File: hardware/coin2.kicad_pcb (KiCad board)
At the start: 2 copper layers, 140 x 40 mm, 69 parts, among them J1 Conn_01x04, J2 Conn_01x03, T1 TestPoint_THTPad_3.0x3.0mm_Dr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, T12 TestPoint_THTPad_3.0x3.0mm_Dr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, T13 TestPoint_THTPad_3.0x3.0mm_Dr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, T14 TestPoint_THTPad_3.0x3.0mm_Dr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, T15 TestPoint_THTPad_3.0x3.0mm_Dr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, T16 TestPoint_THTPad_3.0x3.0mm_Dr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, T18 TestPoint_THTPad_3.0x3.0mm_Dr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, T19 TestPoint_THTPad_3.0x3.0mm_Dr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, T20 TestPoint_THTPad_3.0x3.0mm_Dr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, T21 TestPoint_THTPad_3.0x3.0mm_Dr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, T22 TestPoint_THTPad_3.0x3.0mm_Dr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, T41 TestPoint_THTPad_D1.0mm_Drill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, T42 TestPoint_THTPad_D1.0mm_Drill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, T43 TestPoint_THTPad_D1.0mm_Drill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, T44 TestPoint_THTPad_D1.0mm_Drill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, T45 TestPoint_THTPad_D1.0mm_Drill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, T46 TestPoint_THTPad_D1.0mm_Drill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, T47 TestPoint_THTPad_D1.0mm_Drill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, T48 TestPoint_THTPad_D1.0mm_Drill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, T49 TestPoint_THTPad_D1.0mm_Drill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, T50 TestPoint_THTPad_D1.0mm_Drill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, T51 TestPoint_THTPad_D1.0mm_Drill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, T51 TestPoint_THTPad_D2.0mm_Drill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, T52 TestPoint_THTPad_D1.0mm_Drill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, T52 TestPoint_THTPad_D2.0mm_Drill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, T53 TestPoint_THTPad_D2.0mm_Drill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, T54 TestPoint_THTPad_D2.0mm_Drill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, T55 TestPoint_THTPad_D2.0mm_Drill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, T56 TestPoint_THTPad_D2.0mm_Drill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, U1 WCH CH32V003F4U6

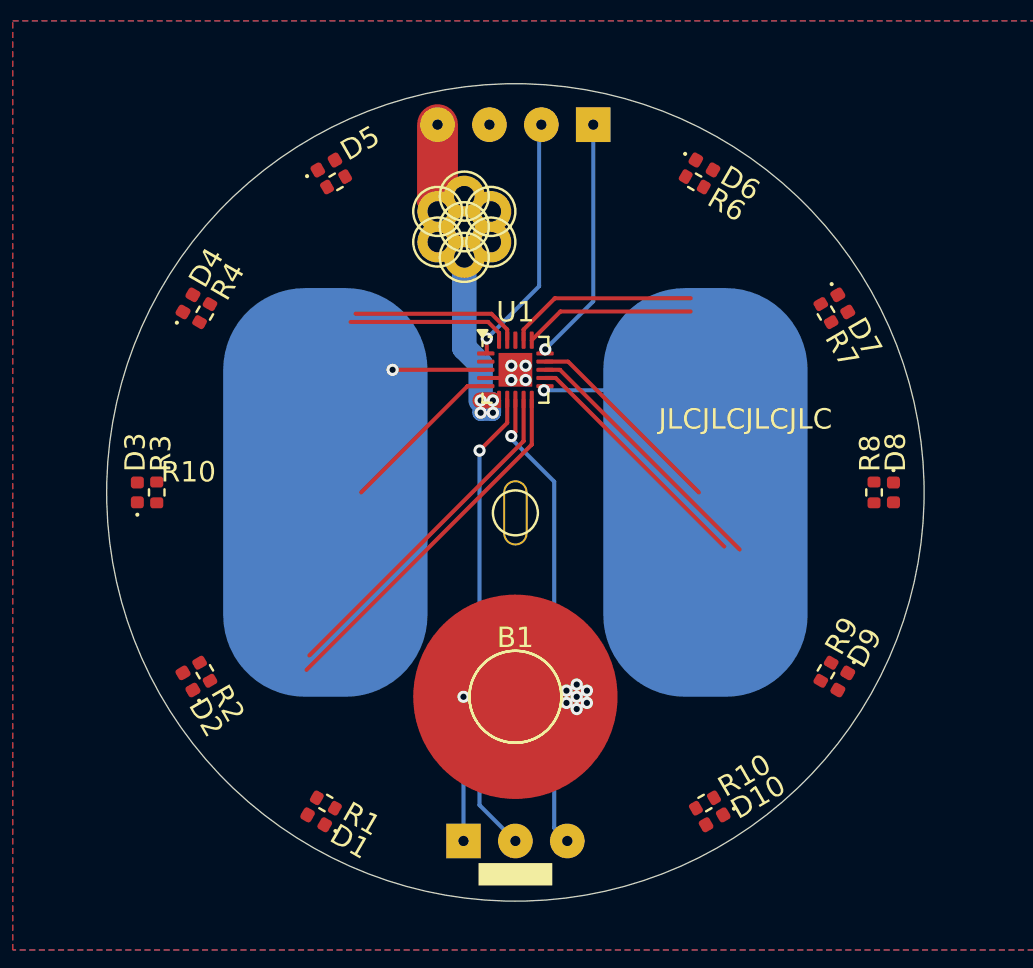
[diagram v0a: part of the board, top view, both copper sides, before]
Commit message: route and DRC the new board
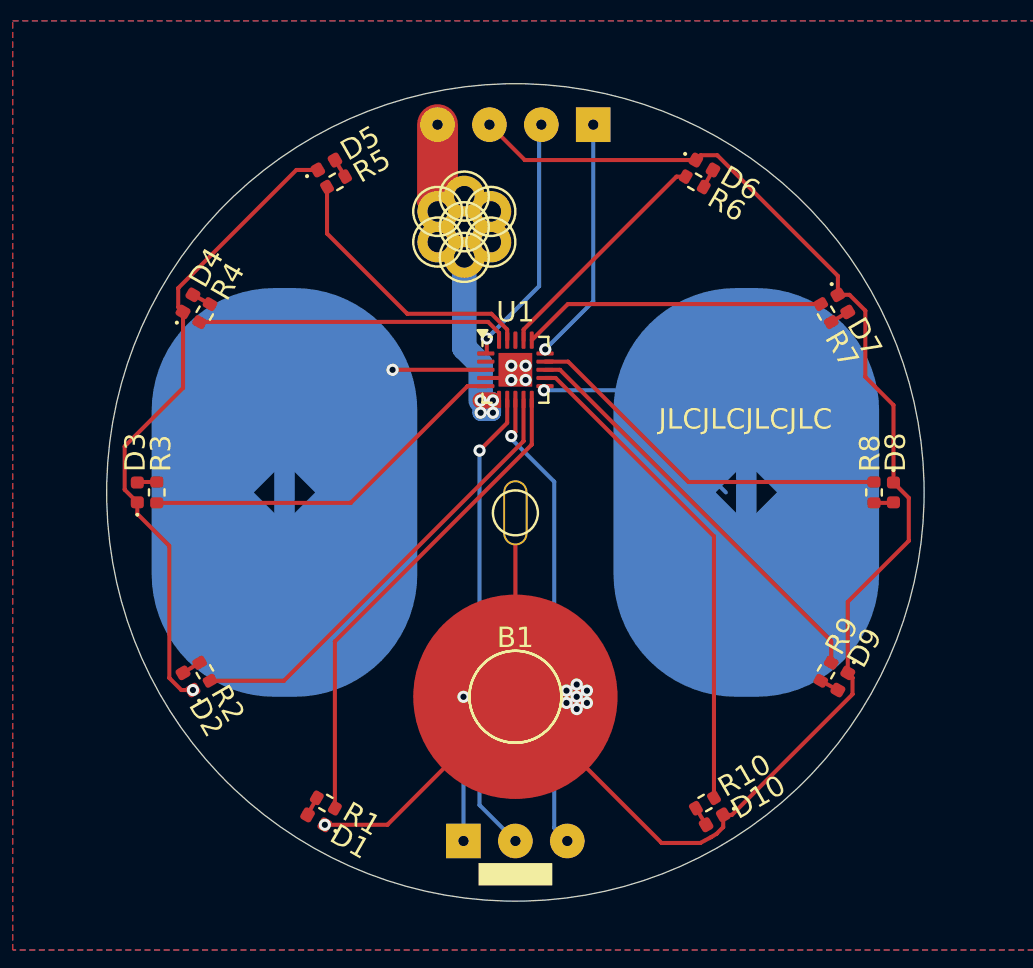
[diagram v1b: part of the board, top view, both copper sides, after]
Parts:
- removed the R10 at (32.5, 50.0)
- added R5: 47R, Resistor_SMD:R_0402_1005Metric, F.Cu at (41.2, 34.8)
- moved R3 17.6 mm to (32.5, 50.0), turned to 90 degrees
- moved S1 2.00 mm to (38.0, 50.0)
- moved S2 2.00 mm to (62.0, 50.0)
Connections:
- D3 pad 2: Net-(D10-A) (its old number) -> Net-(D3-A)
- D4 pad 1: (no net) -> GND
- D4 pad 2: (no net) -> Net-(D4-A)
- D5 pad 1: (no net) -> GND
- D5 pad 2: (no net) -> Net-(D5-A)
- R1 pad 1: /LED8 -> /LED1
- R10 pad 1: /LED6 -> /LED10
- R2 pad 1: /LED9 -> /LED2
- R3 pad 1: (no net) -> /LED3
- R3 pad 2: (no net) -> Net-(D3-A)
- R4 pad 1: (no net) -> /LED4
- R4 pad 2: (no net) -> Net-(D4-A)
- R6 pad 1: /LED2 -> /LED6
- R7 pad 1: /LED3 -> /LED7
- R8 pad 1: /LED4 -> /LED8
- R9 pad 1: /LED5 -> /LED9
- U1 pad 21: VSS -> GND
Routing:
- net GND: track 9.61 -> 129.1 mm, vias 12 -> 14
- net /LED10: track 12.2 -> 24.3 mm
- net /LED3: track 8.25 -> 18.5 mm
- net /LED8: track 10.2 -> 18.5 mm
- net /LED4: track 7.84 -> 15.2 mm
- net /LED9: track 13.2 -> 20.6 mm
- net /LED7: track 8.35 -> 14.9 mm
- net /LED1: track 17.8 -> 24.0 mm
- net /LED2: track 16.9 -> 22.2 mm
- net /LED5: track 8.26 -> 13.6 mm
- net /LED6: track 9.33 -> 11.6 mm
- net Net-(D3-A): track 0.00 -> 0.96 mm
- net Net-(D8-A): track 0.00 -> 0.96 mm
- net Net-(D7-A): track 0.00 -> 0.95 mm
- net Net-(D10-A): track 0.00 -> 0.95 mm
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
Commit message: cleanup some hole locations etc.
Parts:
- removed T41, T47: TestPoint_THTPad_D1.0mm_Drill0.5mm, TestPoint:TestPoint_THTPad_D1.0mm_Drill0.5mm
- moved T46 0.25 mm to (159.5, 66.0)
- moved T48 0.25 mm to (140.5, 66.0)
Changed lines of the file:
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@@
 		)
 	)
-	(footprint "TestPoint:TestPoint_THTPad_D1.0mm_Drill0.5mm"
-		(layer "F.Cu")
-		(at 150 68.5 -120)
-		(descr "THT pad as test Point, diameter 1.0mm, hole diameter 0.5mm")
-		(tags "test point THT pad")
-		(property "Reference" "T47"
-			(at 0 -2.398 -120)
-			(layer "F.SilkS")
-			(hide yes)
-			(effects
-				(font
-					(size 1 1)
-					(thickness 0.15)
-				)
-			)
-		)
-		(property "Value" "TestPoint_THTPad_D1.0mm_Drill0.5mm"
-			(at 0 2.549999 -120)
-			(layer "F.Fab")
-			(hide yes)
-			(effects
-				(font
-					(size 1 1)
-					(thickness 0.15)
-				)
-			)
-		)
-		(property "Footprint" "TestPoint:TestPoint_THTPad_D1.0mm_Drill0.5mm"
-			(at 0 0 -120)
-			(unlocked yes)
-			(layer "F.Fab")
-			(hide yes)
-			(effects
-				(font
-					(size 1.27 1.27)
-					(thickness 0.15)
-				)
-			)
-		)
-		(property "Datasheet" ""
-			(at 0 0 -120)
-			(unlocked yes)
-			(layer "F.Fab")
-			(hide yes)
-			(effects
-				(font
-					(size 1.27 1.27)
-					(thickness 0.15)
-				)
-			)
-		)
-		(property "Description" ""
-			(at 0 0 -120)
-			(unlocked yes)
-			(layer "F.Fab")
-			(hide yes)
-			(effects
-				(font
-					(size 1.27 1.27)
-					(thickness 0.15)
-				)
-			)
-		)
-		(attr board_only exclude_from_pos_files exclude_from_bom)
-		(fp_circle
-			(center 0 0)
-			(end 0.4 0)
-			(stroke
-				(width 0.05)
-				(type solid)
-			)
-			(fill none)
-			(layer "F.CrtYd")
-		)
-		(pad "1" thru_hole circle
-			(at 0 0 240)
-			(size 0.6 0.6)
-			(drill 0.5)
-			(layers "*.Cu" "*.Mask")
-			(remove_unused_layers no)
-			(net 2 "GND")
-		)
-	)
 	(footprint "Resistor_SMD:R_0402_1005Metric"
 		(layer "F.Cu")
@@
 		)
 		(property "Value" "LED"
-			(at 0 1.169999 120)
+			(at -0.000001 1.169999 120)
 			(layer "F.Fab")
 			(effects
@@
 		)
 		(property "Value" "47R"
-			(at 0 1.169999 120)
+			(at -0.000001 1.169999 120)
 			(layer "F.Fab")
 			(effects
@@
 	(footprint "TestPoint:TestPoint_THTPad_D1.0mm_Drill0.5mm"
 		(layer "F.Cu")
-		(at 150 31.5 60)
-		(descr "THT pad as test Point, diameter 1.0mm, hole diameter 0.5mm")
-		(tags "test point THT pad")
-		(property "Reference" "T41"
-			(at 0 -2.398 60)
-			(layer "F.SilkS")
-			(hide yes)
-			(effects
-				(font
-					(size 1 1)
-					(thickness 0.15)
-				)
-			)
-		)
-		(property "Value" "TestPoint_THTPad_D1.0mm_Drill0.5mm"
-			(at 0 2.549999 60)
-			(layer "F.Fab")
-			(hide yes)
-			(effects
-				(font
-					(size 1 1)
-					(thickness 0.15)
-				)
-			)
-		)
-		(property "Footprint" "TestPoint:TestPoint_THTPad_D1.0mm_Drill0.5mm"
-			(at 0 0 60)
-			(unlocked yes)
-			(layer "F.Fab")
-			(hide yes)
-			(effects
-				(font
-					(size 1.27 1.27)
-					(thickness 0.15)
-				)
-			)
-		)
-		(property "Datasheet" ""
-			(at 0 0 60)
-			(unlocked yes)
-			(layer "F.Fab")
-			(hide yes)
-			(effects
-				(font
-					(size 1.27 1.27)
-					(thickness 0.15)
-				)
-			)
-		)
-		(property "Description" ""
-			(at 0 0 60)
-			(unlocked yes)
-			(layer "F.Fab")
-			(hide yes)
-			(effects
-				(font
-					(size 1.27 1.27)
-					(thickness 0.15)
-				)
-			)
-		)
-		(attr board_only exclude_from_pos_files exclude_from_bom)
-		(fp_circle
-			(center 0 0)
-			(end 0.4 0)
-			(stroke
-				(width 0.05)
-				(type solid)
-			)
-			(fill none)
-			(layer "F.CrtYd")
-		)
-		(pad "1" thru_hole circle
-			(at 0 0 60)
-			(size 0.6 0.6)
-			(drill 0.5)
-			(layers "*.Cu" "*.Mask")
-			(remove_unused_layers no)
-			(net 2 "GND")
-		)
-	)
-	(footprint "TestPoint:TestPoint_THTPad_D1.0mm_Drill0.5mm"
-		(layer "F.Cu")
 		(at 131.5 50 150)
 		(descr "THT pad as test Point, diameter 1.0mm, hole diameter 0.5mm")
@@
 		(tags "resistor")
 		(property "Reference" "R10"
-			(at -1 0.2 210)
+			(at -1 0.2 -150)
 			(layer "F.SilkS")
 			(effects
@@
 		(tags "LED")
 		(property "Reference" "D6"
-			(at 0.999999 -0.1 330)
+			(at 0.999999 -0.1 -30)
 			(layer "F.SilkS")
 			(effects
@@
 		(tags "resistor")
 		(property "Reference" "R8"
-			(at -1 0.2 270)
+			(at -1 0.2 -90)
 			(layer "F.SilkS")
 			(effects
@@
 	(footprint "TestPoint:TestPoint_THTPad_D1.0mm_Drill0.5mm"
 		(layer "F.Cu")
-		(at 140.75 66.021469 -150)
+		(at 140.5 66.021469 -150)
 		(descr "THT pad as test Point, diameter 1.0mm, hole diameter 0.5mm")
 		(tags "test point THT pad")
 		(property "Reference" "T48"
-			(at 0 -2.397999 -150)
+			(at 0 -2.397999 30)
 			(layer "F.SilkS")
 			(hide yes)
@@
 		)
 		(property "Value" "TestPoint_THTPad_D1.0mm_Drill0.5mm"
-			(at 0 2.55 -150)
+			(at 0 2.55 30)
 			(layer "F.Fab")
 			(hide yes)
@@
 		(tags "LED")
 		(property "Reference" "D10"
-			(at -0.999999 -0.1 210)
+			(at -0.999999 -0.1 -150)
 			(layer "F.SilkS")
 			(effects
@@
 		(tags "resistor")
 		(property "Reference" "R6"
-			(at 1 0.2 330)
+			(at 1 0.2 -30)
 			(layer "F.SilkS")
 			(effects
@@
 	(footprint "TestPoint:TestPoint_THTPad_D1.0mm_Drill0.5mm"
 		(layer "F.Cu")
-		(at 159.25 66.021469 -90)
+		(at 159.5 66.021469 -90)
 		(descr "THT pad as test Point, diameter 1.0mm, hole diameter 0.5mm")
 		(tags "test point THT pad")
 		(property "Reference" "T46"
-			(at -0.000001 -2.398 -90)
+			(at -0.000001 -2.398 90)
 			(layer "F.SilkS")
 			(hide yes)
@@
 		)
 		(property "Value" "TestPoint_THTPad_D1.0mm_Drill0.5mm"
-			(at -0.000001 2.55 -90)
+			(at -0.000001 2.55 90)
 			(layer "F.Fab")
 			(hide yes)
@@
 		(tags "resistor")
 		(property "Reference" "R9"
-			(at -1 0.2 240)
+			(at -1 0.2 -120)
 			(layer "F.SilkS")
 			(effects
@@
 		)
 		(property "Value" "LED"
-			(at 0 1.169999 30)
+			(at -0.000001 1.169999 30)
 			(layer "F.Fab")
 			(effects
@@
 		(tags "LED")
 		(property "Reference" "D9"
-			(at -1 -0.100001 240)
+			(at -1 -0.100001 -120)
 			(layer "F.SilkS")
 			(effects
@@
 		(tags "resistor")
 		(property "Reference" "R7"
-			(at 0.999999 0.200001 300)
+			(at 0.999999 0.200001 -60)
 			(layer "F.SilkS")
 			(effects
@@
 		(tags "LED")
 		(property "Reference" "D7"
-			(at 1 -0.100001 300)
+			(at 1 -0.100001 -60)
 			(layer "F.SilkS")
 			(effects
@@
 		(tags "LED")
 		(property "Reference" "D8"
-			(at -1 -0.1 270)
+			(at -1 -0.1 -90)
 			(layer "F.SilkS")
 			(effects

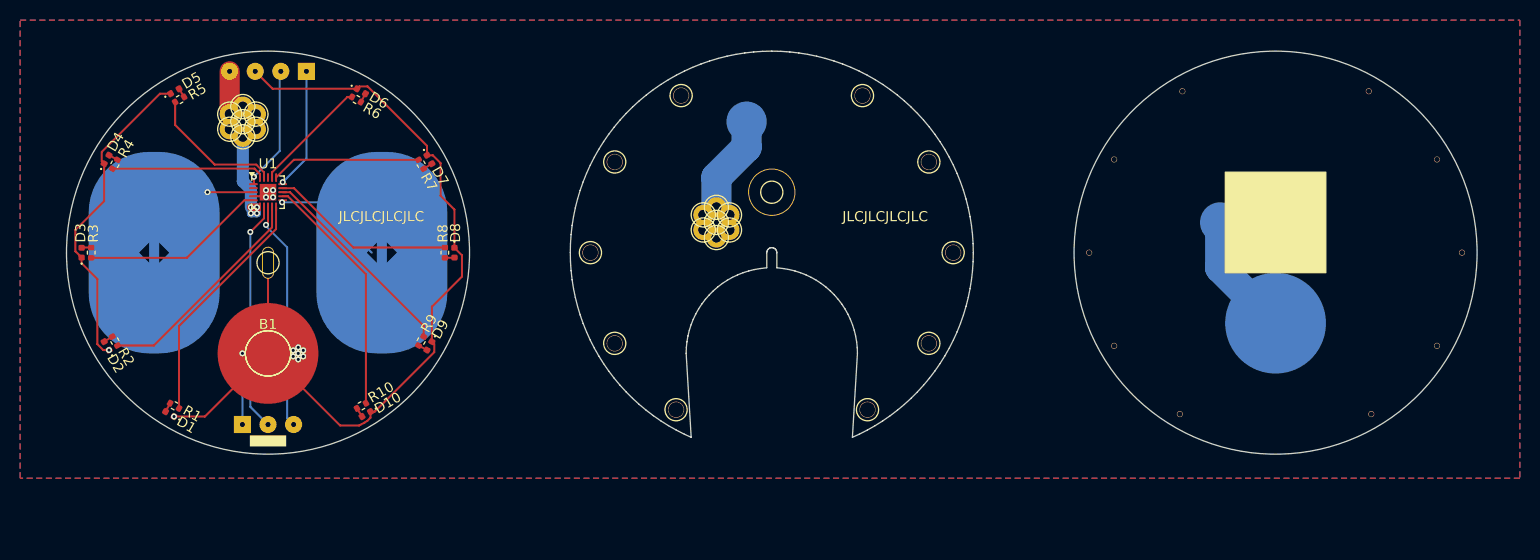
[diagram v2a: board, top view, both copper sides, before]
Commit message: add bypass caps, tweak clearance holes
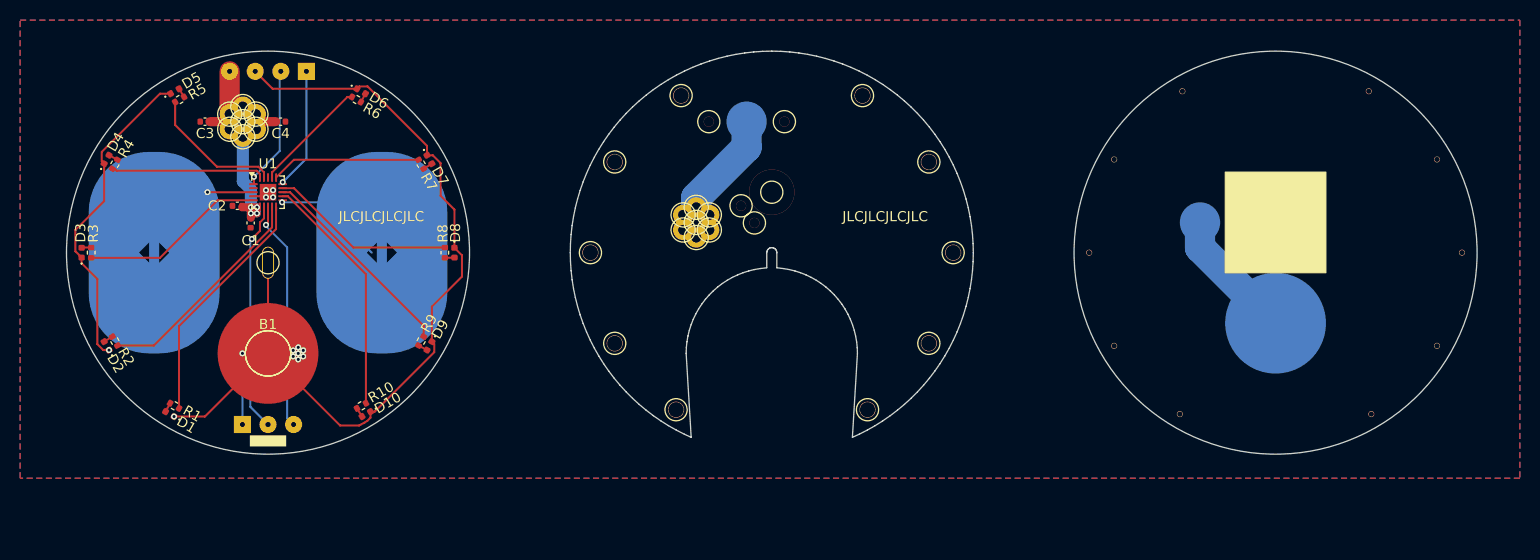
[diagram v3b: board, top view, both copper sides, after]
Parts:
- added C1: 10n, Capacitor_SMD:C_0402_1005Metric, F.Cu at (48.3, 47.0)
- added C2: 10n, Capacitor_SMD:C_0402_1005Metric, F.Cu at (47.0, 45.4)
- added C3: 10n, Capacitor_SMD:C_0402_1005Metric, F.Cu at (43.8, 37.0)
- added C4: 10n, Capacitor_SMD:C_0402_1005Metric, F.Cu at (51.2, 37.0)
- added T21: TestPoint_THTPad_3.0x3.0mm_Drill1.5mm, TestPoint:TestPoint_THTPad_3.0x3.0mm_Drill1.5mm, F.Cu at (97.0, 45.4)
- added T21: TestPoint_THTPad_3.0x3.0mm_Drill1.5mm, TestPoint:TestPoint_THTPad_3.0x3.0mm_Drill1.5mm, F.Cu at (101.2, 37.0)
- added T21: TestPoint_THTPad_3.0x3.0mm_Drill1.5mm, TestPoint:TestPoint_THTPad_3.0x3.0mm_Drill1.5mm, F.Cu at (93.8, 37.0)
- added T21: TestPoint_THTPad_3.0x3.0mm_Drill1.5mm, TestPoint:TestPoint_THTPad_3.0x3.0mm_Drill1.5mm, F.Cu at (98.3, 47.0)
- moved REF** 2.00 mm to (142.5, 47.0)
- moved T51 2.00 mm to (92.5, 45.5)
- moved T51 2.00 mm to (92.5, 47.0)
- moved T52 2.00 mm to (93.8, 46.2)
- moved T53 2.00 mm to (93.8, 47.8)
- moved T54 2.00 mm to (92.5, 48.5)
- moved T55 2.00 mm to (91.2, 47.8)
- moved T56 2.00 mm to (91.2, 46.2)
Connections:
- U1 pad 21: GND -> VSS
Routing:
- net +3V0: track 41.3 -> 50.8 mm

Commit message: change connectors from 2.54 to 1.27mm spacing, add decoupling
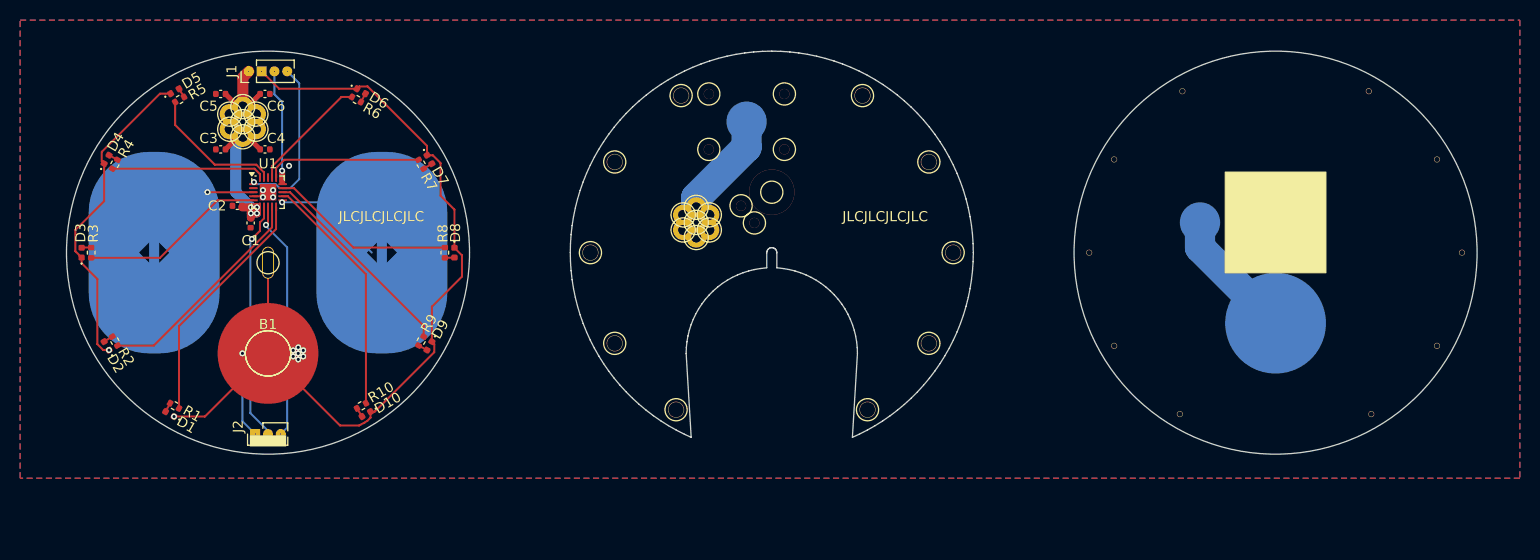
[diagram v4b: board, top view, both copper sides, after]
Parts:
- added C5: 10n, Capacitor_SMD:C_0402_1005Metric, F.Cu at (45.3, 34.2)
- added C6: 10n, Capacitor_SMD:C_0402_1005Metric, F.Cu at (49.7, 34.2)
- added T21: TestPoint_THTPad_3.0x3.0mm_Drill1.5mm, TestPoint:TestPoint_THTPad_3.0x3.0mm_Drill1.5mm, F.Cu at (93.8, 34.2)
- added T21: TestPoint_THTPad_3.0x3.0mm_Drill1.5mm, TestPoint:TestPoint_THTPad_3.0x3.0mm_Drill1.5mm, F.Cu at (101.2, 34.2)
- J1: footprint Connector_PinHeader_2.54mm:PinHeader_1x04_P2.54mm_Vertical -> Connector_PinHeader_1.27mm:PinHeader_1x04_P1.27mm_Vertical; moved to F.Cu
- J2: footprint Connector_PinHeader_2.54mm:PinHeader_1x03_P2.54mm_Vertical -> Connector_PinHeader_1.27mm:PinHeader_1x03_P1.27mm_Vertical; moved to F.Cu
- moved J1 5.72 mm to (48.1, 32.0)
- moved C3 3.16 mm to (45.3, 39.8)
- moved C4 3.16 mm to (49.7, 39.8)
- moved T21 2.75 mm to (101.2, 39.8)
- moved T21 2.75 mm to (93.8, 39.8)
- moved J2 1.58 mm to (48.7, 68.0), turned to 90 degrees
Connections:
- J1 pad 1: /SWIO -> +3V0
- J1 pad 2: /NRST -> GND
- J1 pad 3: GND -> /SWIO
- J1 pad 4: +3V0 -> /NRST
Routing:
- net +3V0: track 50.8 -> 58.2 mm
- net /NRST: track 12.3 -> 16.5 mm
- net /TX: track 22.9 -> 23.8 mm
- net /RX: track 22.8 -> 23.8 mm
- net /SWIO: track 12.2 -> 11.3 mm
- net /LED7: track 14.9 -> 15.4 mm
- net GND: track 129.1 -> 129.2 mm, vias 14 -> 15
